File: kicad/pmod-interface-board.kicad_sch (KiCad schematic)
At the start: 30 parts, among them J1 PMOD Connector 1, J2 PMOD Connector 2, J4 GB Cart Breakout, U1 74HCT541, U2 74HCT541, U3 74HC595, U4 74HC595, U5 74HC595, U6 74HC597

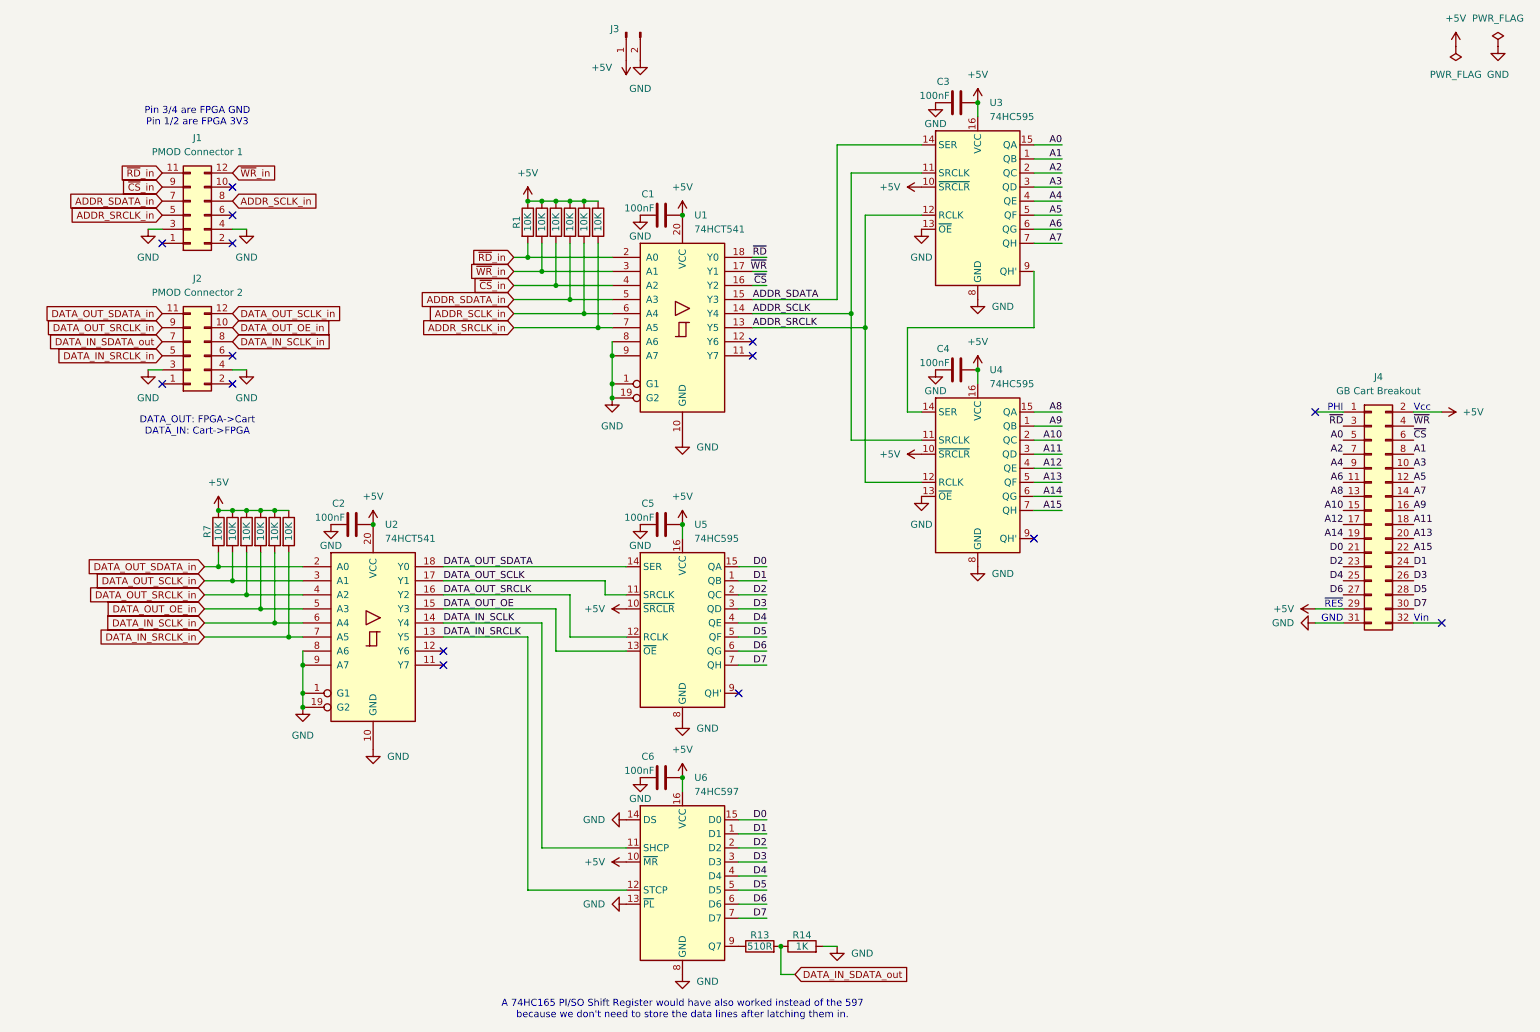
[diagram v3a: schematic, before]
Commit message: kicad: moved pins for better connectivity and renamed srclk to sclk
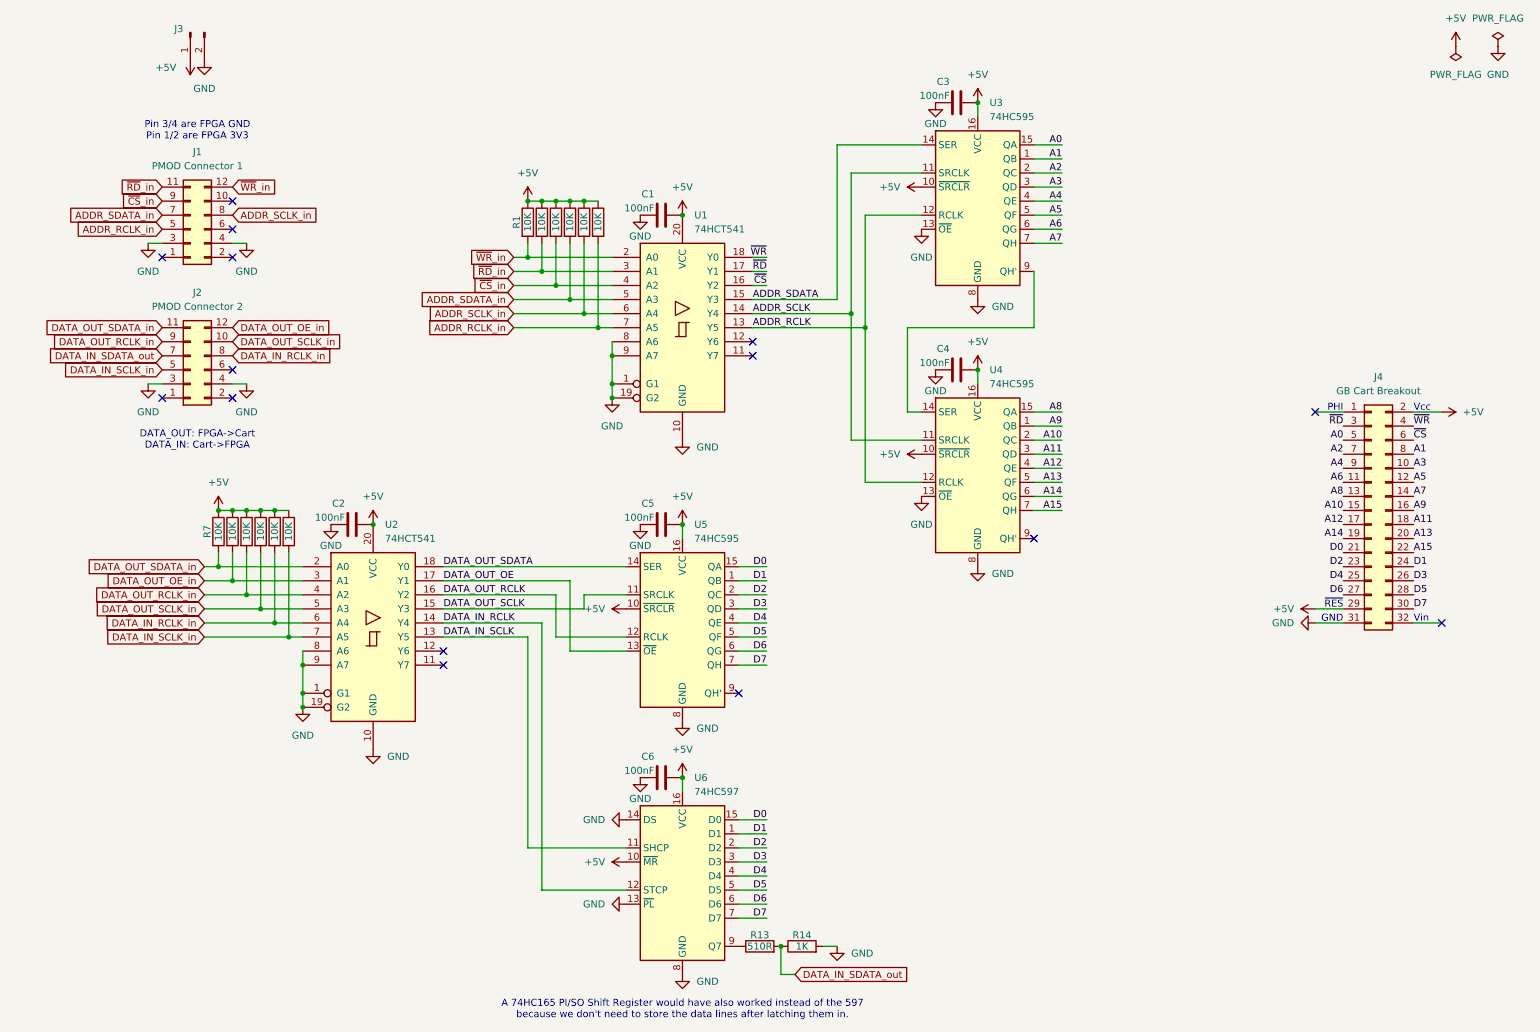
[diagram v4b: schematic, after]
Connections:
- net DATA_IN_SRCLK_in is gone; now on net DATA_IN_SCLK_in: J2.5 (Pin_5), R12.2, U2.7 (A5)
- net DATA_IN_SCLK: now also U2.13 (Y5); no longer U2.14 (Y4)
- net DATA_IN_SCLK_in: no longer J2.8 (Pin_8), R11.2, U2.6 (A4)
- net DATA_OUT_OE: now also U2.17 (Y1); no longer U2.15 (Y3)
- net DATA_OUT_OE_in: now also J2.12 (Pin_12), R8.2, U2.3 (A1); no longer J2.10 (Pin_10), R10.2, U2.5 (A3)
- net DATA_OUT_SCLK: now also U2.15 (Y3); no longer U2.17 (Y1)
- net DATA_OUT_SCLK_in: now also J2.10 (Pin_10), R10.2, U2.5 (A3); no longer J2.12 (Pin_12), R8.2, U2.3 (A1)
- net ~{RD}: now also U1.17 (Y1); no longer U1.18 (Y0)
- net ~{RD}_in: now also R2.2, U1.3 (A1); no longer R1.2, U1.2 (A0)
- net ~{WR}: now also U1.18 (Y0); no longer U1.17 (Y1)
- net ~{WR}_in: now also R1.2, U1.2 (A0); no longer R2.2, U1.3 (A1)
- net ADDR_SRCLK renamed ADDR_RCLK
- net ADDR_SRCLK_in renamed ADDR_RCLK_in
- net DATA_IN_SRCLK renamed DATA_IN_RCLK
- net DATA_IN_RCLK: now also U2.14 (Y4); no longer U2.13 (Y5)
- net DATA_OUT_SRCLK renamed DATA_OUT_RCLK
- net DATA_OUT_SRCLK_in renamed DATA_OUT_RCLK_in
- new net DATA_IN_RCLK_in: J2.8 (Pin_8), R11.2, U2.6 (A4)
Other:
- moved on the sheet: J1, J2, J3

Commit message: kicad: added custom gbcart connector footprint and updated schematics
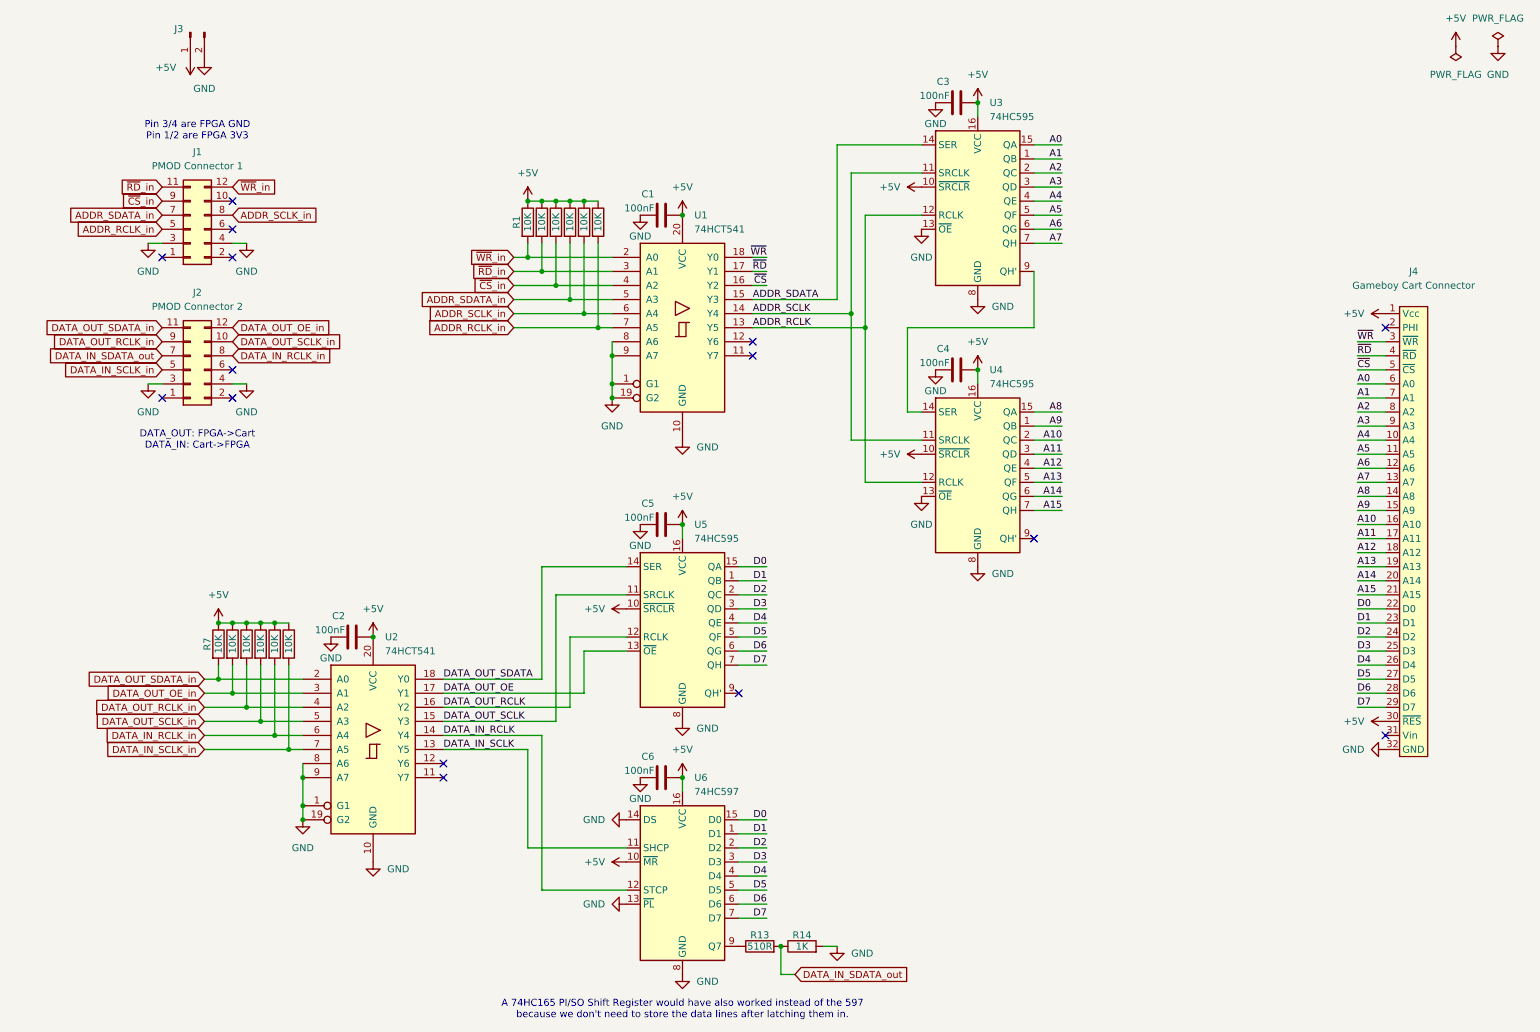
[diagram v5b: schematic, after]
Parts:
- removed J4: GB Cart Breakout, Connector_PinHeader_2.54mm:PinHeader_2x16_P2.54mm_Vertical, symbol Connector_Generic:Conn_02x16_Odd_Even
- added J4: Gameboy Cart Connector, pmod-interface-board:GBCartConnector, symbol pmod-interface-board:GBCartConnector
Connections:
- net +5V: now also J4.1 (Vcc), J4.30 (~{RES})
- net A0: now also J4.6 (A0)
- net A1: now also J4.7 (A1)
- net A10: now also J4.16 (A10)
- net A11: now also J4.17 (A11)
- net A12: now also J4.18 (A12)
- net A13: now also J4.19 (A13)
- net A14: now also J4.20 (A14)
- net A15: now also J4.21 (A15)
- net A2: now also J4.8 (A2)
- net A3: now also J4.9 (A3)
- net A4: now also J4.10 (A4)
- net A5: now also J4.11 (A5)
- net A6: now also J4.12 (A6)
- net A7: now also J4.13 (A7)
- net A8: now also J4.14 (A8)
- net A9: now also J4.15 (A9)
- net D0: now also J4.22 (D0)
- net D1: now also J4.23 (D1)
- net D2: now also J4.24 (D2)
- net D3: now also J4.25 (D3)
- net D4: now also J4.26 (D4)
- net D5: now also J4.27 (D5)
- net D6: now also J4.28 (D6)
- net D7: now also J4.29 (D7)
- net GND: now also J4.32 (GND)
- net ~{CS}: now also J4.5 (~{CS})
- net ~{RD}: now also J4.4 (~{RD})
- net ~{WR}: now also J4.3 (~{WR})
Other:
- note removed: "GND"
- note removed: "PHI"
- note removed: "Vcc"
- note removed: "Vin"
- note removed: "~{RES}"
- moved on the sheet: C2, R7, U2

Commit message: kicad: fixed resistor footprints
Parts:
- R1, R10, R11, R12, R13, R14, R2, R3, R4, R5, R6, R7, R8, R9: footprint Resistor_THT:R_Axial_DIN0207_L6.3mm_D2.5mm_P7.62mm_Horizontal -> Resistor_THT:R_Axial_DIN0204_L3.6mm_D1.6mm_P5.08mm_Horizontal
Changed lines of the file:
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@@
 			)
 		)
-		(property "Footprint" "Resistor_THT:R_Axial_DIN0207_L6.3mm_D2.5mm_P7.62mm_Horizontal"
+		(property "Footprint" "Resistor_THT:R_Axial_DIN0204_L3.6mm_D1.6mm_P5.08mm_Horizontal"
 			(at 112.522 52.07 90)
 			(effects
@@
 			)
 		)
-		(property "Footprint" "Resistor_THT:R_Axial_DIN0207_L6.3mm_D2.5mm_P7.62mm_Horizontal"
+		(property "Footprint" "Resistor_THT:R_Axial_DIN0204_L3.6mm_D1.6mm_P5.08mm_Horizontal"
 			(at 107.442 52.07 90)
 			(effects
@@
 			)
 		)
-		(property "Footprint" "Resistor_THT:R_Axial_DIN0207_L6.3mm_D2.5mm_P7.62mm_Horizontal"
+		(property "Footprint" "Resistor_THT:R_Axial_DIN0204_L3.6mm_D1.6mm_P5.08mm_Horizontal"
 			(at 56.642 128.27 90)
 			(effects
@@
 			)
 		)
-		(property "Footprint" "Resistor_THT:R_Axial_DIN0207_L6.3mm_D2.5mm_P7.62mm_Horizontal"
+		(property "Footprint" "Resistor_THT:R_Axial_DIN0204_L3.6mm_D1.6mm_P5.08mm_Horizontal"
 			(at 49.022 128.27 90)
 			(effects
@@
 			)
 		)
-		(property "Footprint" "Resistor_THT:R_Axial_DIN0207_L6.3mm_D2.5mm_P7.62mm_Horizontal"
+		(property "Footprint" "Resistor_THT:R_Axial_DIN0204_L3.6mm_D1.6mm_P5.08mm_Horizontal"
 			(at 46.482 128.27 90)
 			(effects
@@
 			)
 		)
-		(property "Footprint" "Resistor_THT:R_Axial_DIN0207_L6.3mm_D2.5mm_P7.62mm_Horizontal"
+		(property "Footprint" "Resistor_THT:R_Axial_DIN0204_L3.6mm_D1.6mm_P5.08mm_Horizontal"
 			(at 51.562 128.27 90)
 			(effects
@@
 			)
 		)
-		(property "Footprint" "Resistor_THT:R_Axial_DIN0207_L6.3mm_D2.5mm_P7.62mm_Horizontal"
+		(property "Footprint" "Resistor_THT:R_Axial_DIN0204_L3.6mm_D1.6mm_P5.08mm_Horizontal"
 			(at 151.13 184.658 90)
 			(effects
@@
 			)
 		)
-		(property "Footprint" "Resistor_THT:R_Axial_DIN0207_L6.3mm_D2.5mm_P7.62mm_Horizontal"
+		(property "Footprint" "Resistor_THT:R_Axial_DIN0204_L3.6mm_D1.6mm_P5.08mm_Horizontal"
 			(at 109.982 52.07 90)
 			(effects
@@
 			)
 		)
-		(property "Footprint" "Resistor_THT:R_Axial_DIN0207_L6.3mm_D2.5mm_P7.62mm_Horizontal"
+		(property "Footprint" "Resistor_THT:R_Axial_DIN0204_L3.6mm_D1.6mm_P5.08mm_Horizontal"
 			(at 143.51 184.658 90)
 			(effects
@@
 			)
 		)
-		(property "Footprint" "Resistor_THT:R_Axial_DIN0207_L6.3mm_D2.5mm_P7.62mm_Horizontal"
+		(property "Footprint" "Resistor_THT:R_Axial_DIN0204_L3.6mm_D1.6mm_P5.08mm_Horizontal"
 			(at 99.822 52.07 90)
 			(effects
@@
 			)
 		)
-		(property "Footprint" "Resistor_THT:R_Axial_DIN0207_L6.3mm_D2.5mm_P7.62mm_Horizontal"
+		(property "Footprint" "Resistor_THT:R_Axial_DIN0204_L3.6mm_D1.6mm_P5.08mm_Horizontal"
 			(at 54.102 128.27 90)
 			(effects
@@
 			)
 		)
-		(property "Footprint" "Resistor_THT:R_Axial_DIN0207_L6.3mm_D2.5mm_P7.62mm_Horizontal"
+		(property "Footprint" "Resistor_THT:R_Axial_DIN0204_L3.6mm_D1.6mm_P5.08mm_Horizontal"
 			(at 104.902 52.07 90)
 			(effects
@@
 			)
 		)
-		(property "Footprint" "Resistor_THT:R_Axial_DIN0207_L6.3mm_D2.5mm_P7.62mm_Horizontal"
+		(property "Footprint" "Resistor_THT:R_Axial_DIN0204_L3.6mm_D1.6mm_P5.08mm_Horizontal"
 			(at 102.362 52.07 90)
 			(effects
@@
 			)
 		)
-		(property "Footprint" "Resistor_THT:R_Axial_DIN0207_L6.3mm_D2.5mm_P7.62mm_Horizontal"
+		(property "Footprint" "Resistor_THT:R_Axial_DIN0204_L3.6mm_D1.6mm_P5.08mm_Horizontal"
 			(at 43.942 128.27 90)
 			(effects

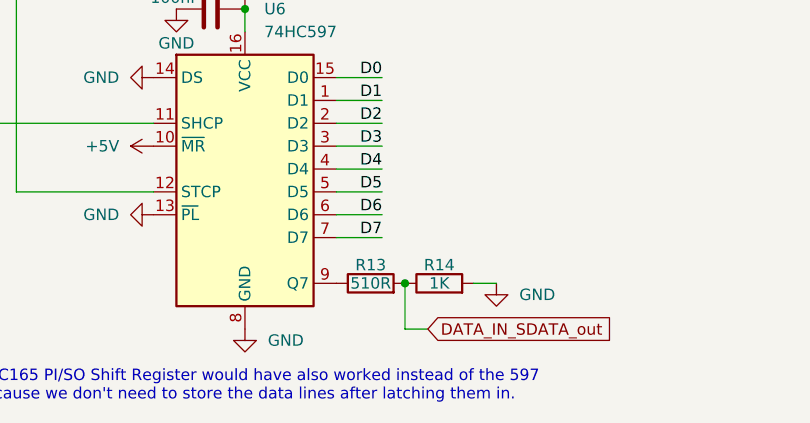
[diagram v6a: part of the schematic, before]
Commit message: kicad: routing completed, sped up resistor divider by lowering values
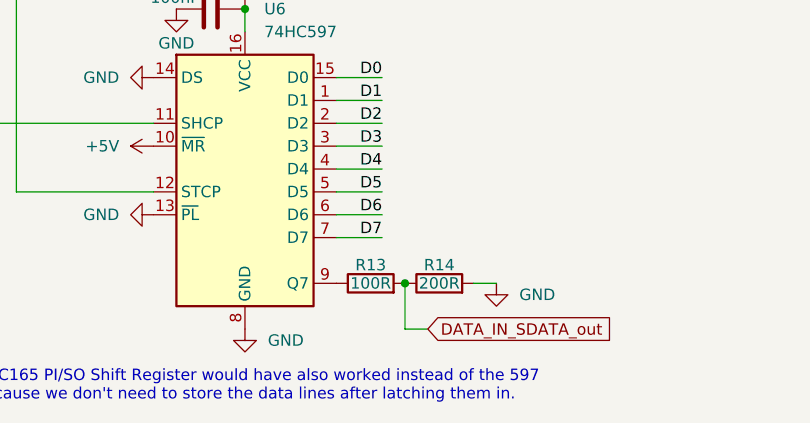
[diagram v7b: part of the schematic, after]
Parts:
- R13: value 510R -> 100R
- R14: value 1K -> 200R
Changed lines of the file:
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@@
 			)
 		)
-		(property "Value" "1K"
+		(property "Value" "200R"
 			(at 151.13 182.88 90)
 			(effects
@@
 			)
 		)
-		(property "Value" "510R"
+		(property "Value" "100R"
 			(at 143.51 182.88 90)
 			(effects

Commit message: kicad: switched out power header and moved pmod connectors closer
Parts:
- J3: footprint Connector_PinHeader_2.54mm:PinHeader_1x02_P2.54mm_Horizontal -> Connector_PinHeader_2.54mm:PinHeader_1x02_P2.54mm_Vertical
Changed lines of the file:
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@@
 			)
 		)
-		(property "Footprint" "Connector_PinHeader_2.54mm:PinHeader_1x02_P2.54mm_Horizontal"
+		(property "Footprint" "Connector_PinHeader_2.54mm:PinHeader_1x02_P2.54mm_Vertical"
 			(at 40.64 17.78 0)
 			(effects
